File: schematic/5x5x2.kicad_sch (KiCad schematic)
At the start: 158 parts, among them J1 SW Debug, J2 USB_C_Receptacle_USB2.0, SW1 SW, SW11 SW, SW12 SW, SW13 SW, SW14 SW, SW15 SW, SW21 SW, SW22 SW, SW23 SW, SW24 SW, SW25 SW, SW31 SW, SW32 SW, SW33 SW, SW34 SW, SW35 SW, SW41 SW, SW42 SW, SW43 SW, SW44 SW, SW45 SW, SW51 SW, SW52 SW, SW53 SW, SW54 SW, SW55 SW, SW6 ALPS_EC11, U1 SRV0504, U2 STM32F103C8, U3 LD1117S33CTR, Y1 16M

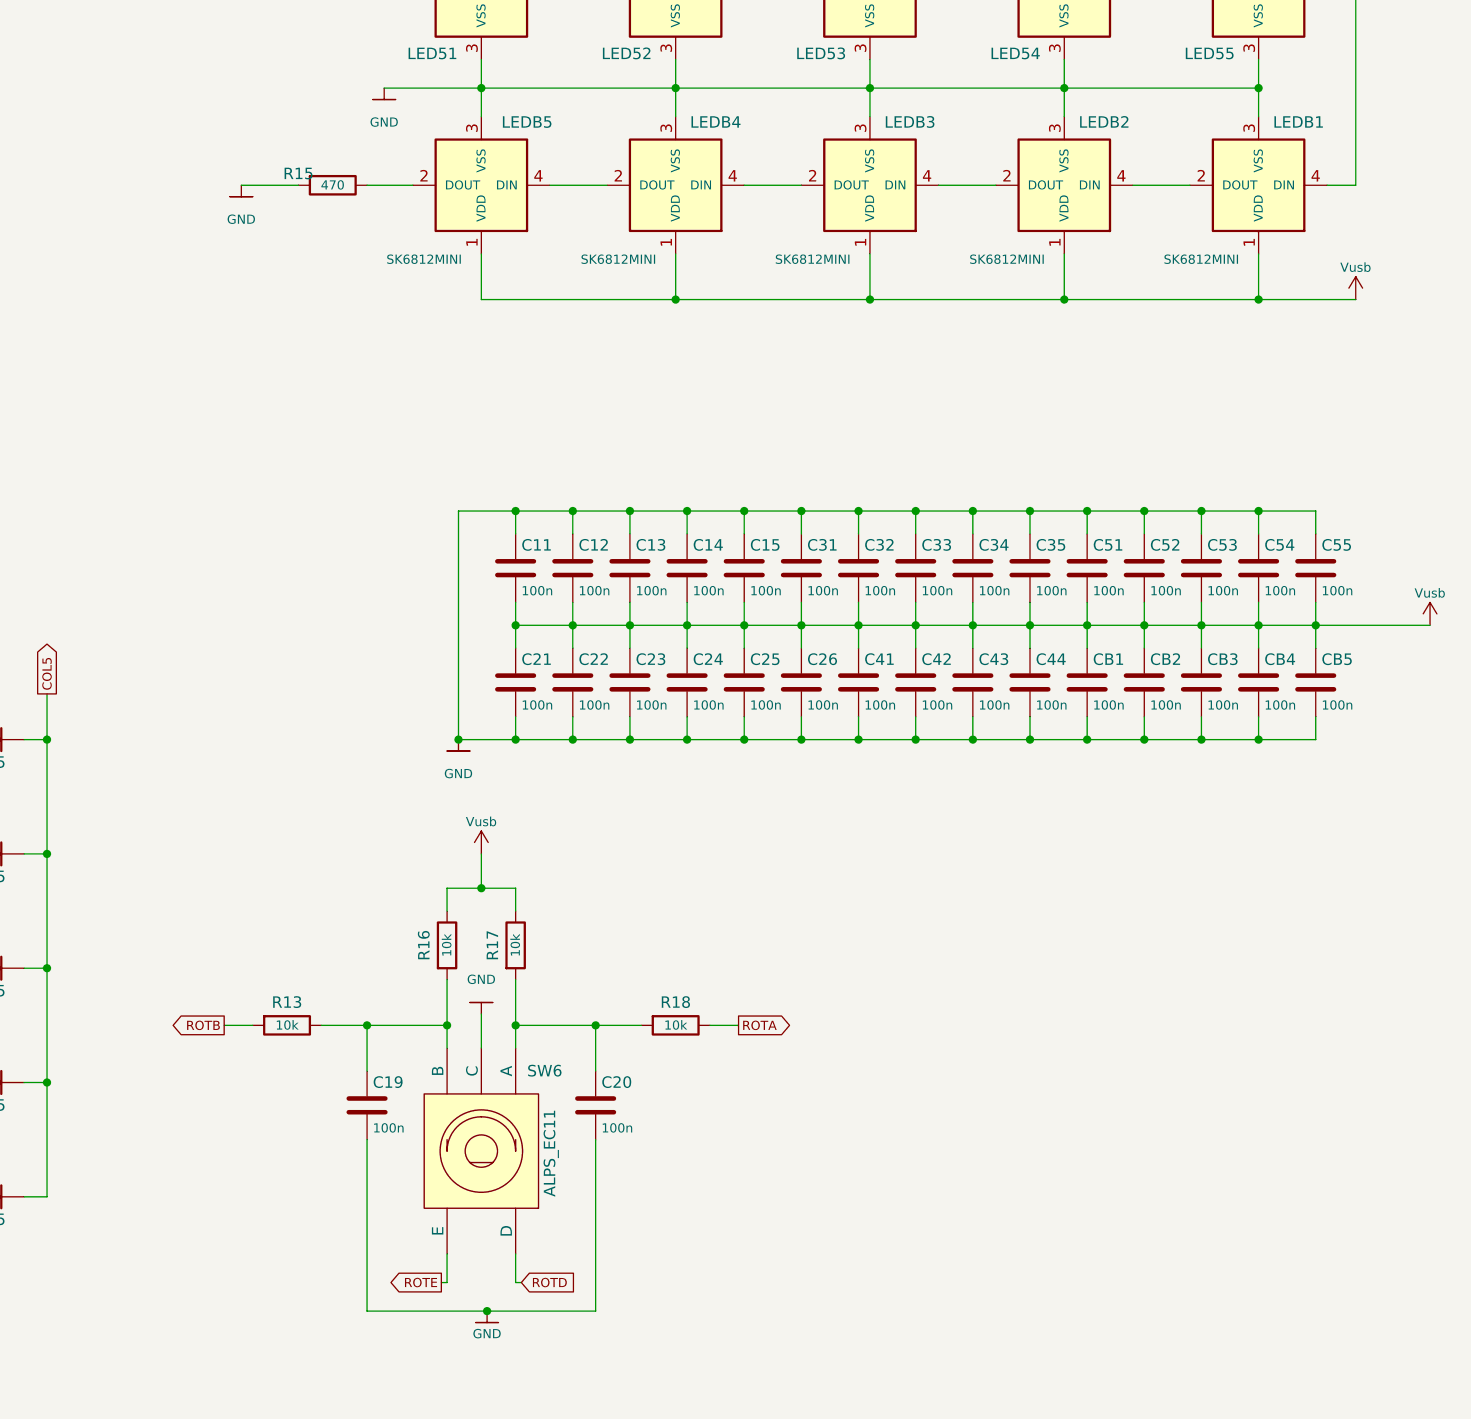
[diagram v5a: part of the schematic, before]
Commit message: Adjusted sk6812 footprint, started routing
Adjusted sk6812 footprint from square cutout to something that is
routable with a mill.

The kailh sockets and leds eat up all the space between the keys. This
means that there is not room for the micro, regulator and usb
receptacle if we stay in a 10x10.

Options:
- Increase size to 11x11 or even 12x12. This would allow for some nice
  mounting holes.

- Make another board beneath the switch board that contains the micro
  and friends.

Lets think about this some more.
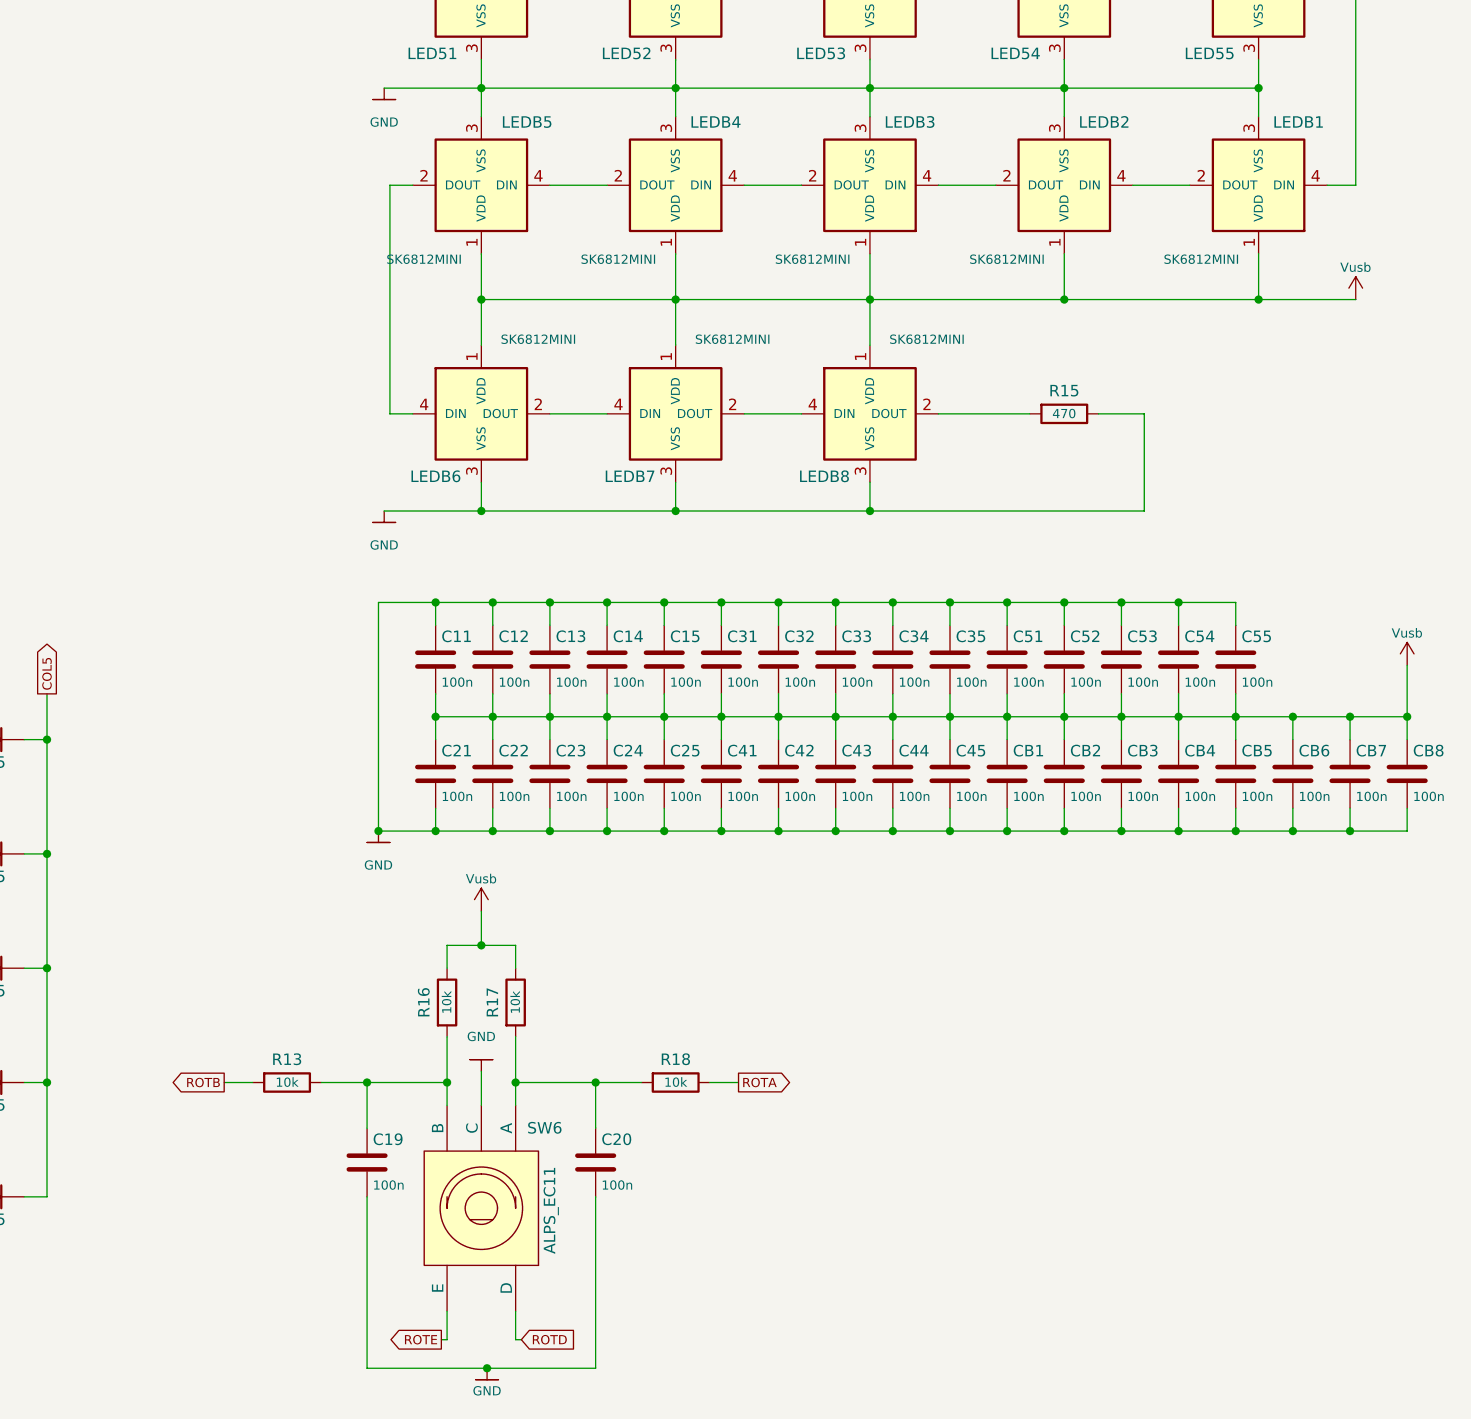
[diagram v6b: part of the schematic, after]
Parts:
- added CB6, CB7, CB8: 100n, Capacitor_SMD:C_0805_2012Metric, symbol Device:C
- added LEDB6, LEDB7, LEDB8: SK6812MINI, footprints:SK6812MINI_rev, symbol SK68xx:SK6812MINI
- C1, C11, C12, C13, C14, C15, C16, C17, C18, C19, C20, C21, C22, C23, C24, C25, C3, C31, C32, C33, C34, C35, C4, C41, C42, C43, C44, C5, C51, C52, C53, C54, C55, C7, C9, CB1, CB2, CB3, CB4, CB5, L1: footprint (none) -> Capacitor_SMD:C_0805_2012Metric
- C10, C2, C6, C8: footprint (none) -> Capacitor_SMD:C_1206_3216Metric
- C45: renamed from C26; footprint (none) -> Capacitor_SMD:C_0805_2012Metric
- C_R1, C_R2, C_R3, R1, R10, R11, R12, R13, R14, R15, R16, R17, R18, R2, R3, R4, R5, R6, R7, R8, R9: footprint (none) -> Resistor_SMD:R_0805_2012Metric
- D1, D2, D3: footprint (none) -> LED_SMD:LED_0805_2012Metric
- J2: footprint (none) -> footprints:USB-C-SMD_TYPE-C-USB-4
- LED11, LED12, LED13, LED14, LED15, LED21, LED22, LED23, LED24, LED25, LED31, LED32, LED33, LED34, LED35, LED41, LED42, LED43, LED44, LED45, LED51, LED52, LED53, LED54, LED55: footprint (none) -> footprints:YS-SK6812MINI-E
- LEDB1, LEDB2, LEDB3, LEDB4, LEDB5: footprint (none) -> footprints:SK6812MINI_rev
- SW1: footprint (none) -> Connector_PinSocket_1.27mm:PinSocket_1x02_P1.27mm_Vertical
- SW11, SW12, SW13, SW14, SW15, SW21, SW22, SW23, SW24, SW25, SW31, SW32, SW33, SW34, SW35, SW41, SW42, SW43, SW44, SW45, SW51, SW52, SW53, SW54, SW55: footprint (none) -> keyswitch:SW_Hotswap_Kailh_MX_1.00u
- SW6: footprint (none) -> footprints:SW-TH_EC11XXXXXXXX
- U1: footprint (none) -> footprints:SOT-23-6_L2.9-W1.6-P0.95-LS2.8-BL
- U2: footprint (none) -> footprints:LQFP-48_L7.0-W7.0-P0.50-LS9.0-BL
- U3: footprint (none) -> footprints:SOT-223-4_L6.5-W3.5-P2.30-LS7.0-BR
- Y1: footprint (none) -> Crystal:Crystal_HC49-U_Vertical
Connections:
- net GND: now also R15.1, CB6.2, CB7.2, CB8.2, LEDB6.3 (VSS), LEDB7.3 (VSS), LEDB8.3 (VSS); no longer R15.2
- net Vusb: now also CB6.1, CB7.1, CB8.1, LEDB6.1 (VDD), LEDB7.1 (VDD), LEDB8.1 (VDD)
- net at LEDB5.2 (DOUT): now also LEDB6.4 (DIN); no longer R15.1
- new net: LEDB8.2 (DOUT), R15.2
- new net: LEDB7.2 (DOUT), LEDB8.4 (DIN)
- new net: LEDB6.2 (DOUT), LEDB7.4 (DIN)
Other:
- moved on the sheet: C11, C12, C13, C14, C15, C19, C20, C21, C22, C23, C24, C25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

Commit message: More routing
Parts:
- renumbered LED25 to LED21, LED24 to LED22, LED22 to LED24, LED21 to LED25, LED45 to LED41, LED44 to LED42, LED42 to LED44, LED41 to LED45
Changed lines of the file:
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@@
   (symbol (lib_id "SK68xx:SK6812MINI-E") (at 355.6 61.595 180) (unit 1)
     (in_bom yes) (on_board yes)
-    (property "Reference" "LED21" (id 0) (at 362.585 54.61 0)
+    (property "Reference" "LED25" (id 0) (at 362.585 54.61 0)
       (effects (font (size 1.27 1.27)) (justify left))
     )
@@
   (symbol (lib_id "SK68xx:SK6812MINI-E") (at 269.24 104.775 180) (unit 1)
     (in_bom yes) (on_board yes)
-    (property "Reference" "LED45" (id 0) (at 276.225 97.79 0)
+    (property "Reference" "LED41" (id 0) (at 276.225 97.79 0)
       (effects (font (size 1.27 1.27)) (justify left))
     )
@@
   (symbol (lib_id "SK68xx:SK6812MINI-E") (at 290.83 61.595 180) (unit 1)
     (in_bom yes) (on_board yes)
-    (property "Reference" "LED24" (id 0) (at 298.45 54.61 0)
+    (property "Reference" "LED22" (id 0) (at 298.45 54.61 0)
       (effects (font (size 1.27 1.27)) (justify left))
     )
@@
   (symbol (lib_id "SK68xx:SK6812MINI-E") (at 290.83 104.775 180) (unit 1)
     (in_bom yes) (on_board yes)
-    (property "Reference" "LED44" (id 0) (at 297.815 97.79 0)
+    (property "Reference" "LED42" (id 0) (at 297.815 97.79 0)
       (effects (font (size 1.27 1.27)) (justify left))
     )
@@
   (symbol (lib_id "SK68xx:SK6812MINI-E") (at 355.6 104.775 180) (unit 1)
     (in_bom yes) (on_board yes)
-    (property "Reference" "LED41" (id 0) (at 362.585 97.79 0)
+    (property "Reference" "LED45" (id 0) (at 362.585 97.79 0)
       (effects (font (size 1.27 1.27)) (justify left))
     )
@@
   (symbol (lib_id "SK68xx:SK6812MINI-E") (at 334.01 61.595 180) (unit 1)
     (in_bom yes) (on_board yes)
-    (property "Reference" "LED22" (id 0) (at 340.995 54.61 0)
+    (property "Reference" "LED24" (id 0) (at 340.995 54.61 0)
       (effects (font (size 1.27 1.27)) (justify left))
     )
@@
   (symbol (lib_id "SK68xx:SK6812MINI-E") (at 334.01 104.775 180) (unit 1)
     (in_bom yes) (on_board yes)
-    (property "Reference" "LED42" (id 0) (at 340.995 97.79 0)
+    (property "Reference" "LED44" (id 0) (at 340.995 97.79 0)
       (effects (font (size 1.27 1.27)) (justify left))
     )
@@
   (symbol (lib_id "SK68xx:SK6812MINI-E") (at 269.24 61.595 180) (unit 1)
     (in_bom yes) (on_board yes)
-    (property "Reference" "LED25" (id 0) (at 276.86 54.61 0)
+    (property "Reference" "LED21" (id 0) (at 276.86 54.61 0)
       (effects (font (size 1.27 1.27)) (justify left))
     )
@@
       (reference "LED15") (unit 1) (value "SK6812MINI-E") (footprint "footprints:YS-SK6812MINI-E")
     )
-    (path "/025174a1-c1b3-43da-9711-d3a3a7ce445e"
+    (path "/f51d1fbb-e25c-4749-bba5-7561a1e13b31"
       (reference "LED21") (unit 1) (value "SK6812MINI-E") (footprint "footprints:YS-SK6812MINI-E")
     )
-    (path "/dd1c2f7a-c2b3-4df2-93b2-04fe1591f702"
+    (path "/3abfbcd0-9099-438c-a966-1761d5740cb1"
       (reference "LED22") (unit 1) (value "SK6812MINI-E") (footprint "footprints:YS-SK6812MINI-E")
     )
@@
       (reference "LED23") (unit 1) (value "SK6812MINI-E") (footprint "footprints:YS-SK6812MINI-E")
     )
-    (path "/3abfbcd0-9099-438c-a966-1761d5740cb1"
+    (path "/dd1c2f7a-c2b3-4df2-93b2-04fe1591f702"
       (reference "LED24") (unit 1) (value "SK6812MINI-E") (footprint "footprints:YS-SK6812MINI-E")
     )
-    (path "/f51d1fbb-e25c-4749-bba5-7561a1e13b31"
+    (path "/025174a1-c1b3-43da-9711-d3a3a7ce445e"
       (reference "LED25") (unit 1) (value "SK6812MINI-E") (footprint "footprints:YS-SK6812MINI-E")
     )
@@
       (reference "LED35") (unit 1) (value "SK6812MINI-E") (footprint "footprints:YS-SK6812MINI-E")
     )
-    (path "/d96937f5-5821-40dc-9935-d17c504b3d87"
+    (path "/0e23ae1d-611b-4654-9b36-886c92306d44"
       (reference "LED41") (unit 1) (value "SK6812MINI-E") (footprint "footprints:YS-SK6812MINI-E")
     )
-    (path "/f1adb53e-37ad-4a2f-81ba-8714ff14ec13"
+    (path "/72abcb82-0f94-41d1-ace4-f1ac54bc9c8d"
       (reference "LED42") (unit 1) (value "SK6812MINI-E") (footprint "footprints:YS-SK6812MINI-E")
     )
@@
       (reference "LED43") (unit 1) (value "SK6812MINI-E") (footprint "footprints:YS-SK6812MINI-E")
     )
-    (path "/72abcb82-0f94-41d1-ace4-f1ac54bc9c8d"
+    (path "/f1adb53e-37ad-4a2f-81ba-8714ff14ec13"
       (reference "LED44") (unit 1) (value "SK6812MINI-E") (footprint "footprints:YS-SK6812MINI-E")
     )
-    (path "/0e23ae1d-611b-4654-9b36-886c92306d44"
+    (path "/d96937f5-5821-40dc-9935-d17c504b3d87"
       (reference "LED45") (unit 1) (value "SK6812MINI-E") (footprint "footprints:YS-SK6812MINI-E")
     )

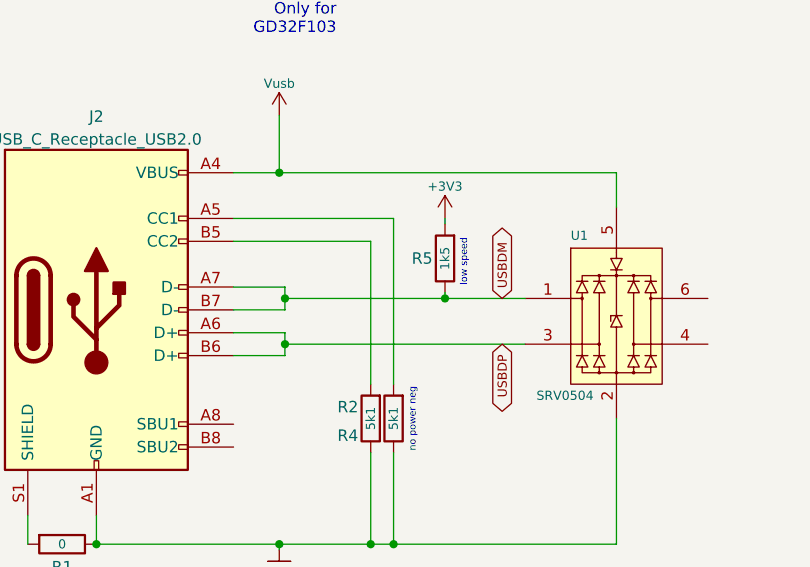
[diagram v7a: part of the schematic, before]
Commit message: Routed for mcu on other pcb
This way we can stay with 2 layers, and optionally have an additional
pcb for just the key switches without kailh holders.
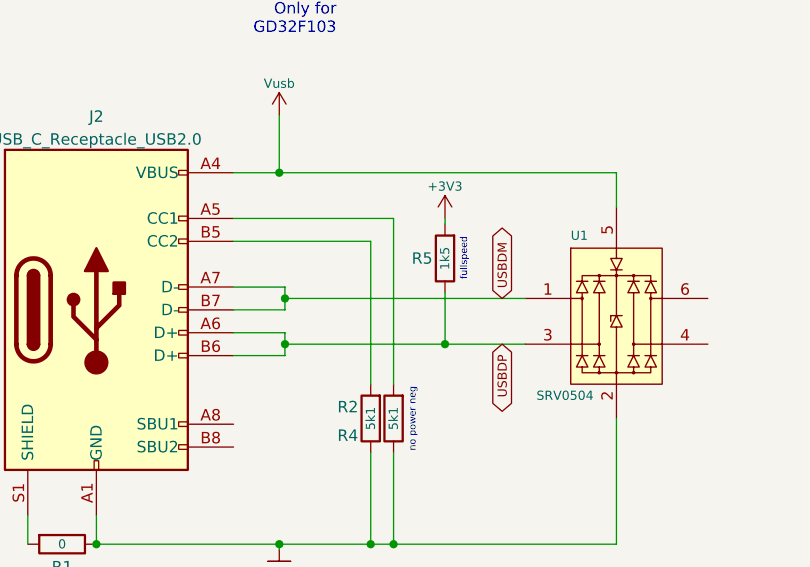
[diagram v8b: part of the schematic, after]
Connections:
- net USBDM: no longer R5.1
- net USBDP: now also R5.1
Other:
- note added: "fullspeed"
- note removed: "low speed"
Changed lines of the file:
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@@
   (junction (at 269.24 160.655) (diameter 0) (color 0 0 0 0)
   )
-  (junction (at 74.295 164.465) (diameter 0) (color 0 0 0 0)
-  )
   (junction (at 182.88 234.95) (diameter 0) (color 0 0 0 0)
   )
@@
   (junction (at 270.51 219.71) (diameter 0) (color 0 0 0 0)
   )
+  (junction (at 74.295 169.545) (diameter 0) (color 0 0 0 0)
+  )
   (junction (at 116.84 265.43) (diameter 0) (color 0 0 0 0)
   )
@@
     (stroke (width 0) (type default) (color 0 0 0 0))
   )
-  (wire (pts (xy 74.295 163.83) (xy 74.295 164.465))
-    (stroke (width 0) (type default) (color 0 0 0 0))
-  )
   (wire (pts (xy 56.515 170.815) (xy 50.8 170.815))
     (stroke (width 0) (type default) (color 0 0 0 0))
@@
     (stroke (width 0) (type default) (color 0 0 0 0))
   )
-  (wire (pts (xy 56.515 164.465) (xy 74.295 164.465))
+  (wire (pts (xy 56.515 164.465) (xy 83.185 164.465))
     (stroke (width 0) (type default) (color 0 0 0 0))
   )
@@
     (stroke (width 0) (type default) (color 0 0 0 0))
   )
-  (wire (pts (xy 74.295 164.465) (xy 83.185 164.465))
-    (stroke (width 0) (type default) (color 0 0 0 0))
-  )
   (wire (pts (xy 55.88 81.28) (xy 55.88 83.82))
     (stroke (width 0) (type default) (color 0 0 0 0))
@@
     (stroke (width 0) (type default) (color 0 0 0 0))
   )
+  (wire (pts (xy 74.295 163.83) (xy 74.295 169.545))
+    (stroke (width 0) (type default) (color 0 0 0 0))
+  )
   (wire (pts (xy 144.78 222.25) (xy 144.78 234.95))
     (stroke (width 0) (type default) (color 0 0 0 0))
@@
     (stroke (width 0) (type default) (color 0 0 0 0))
   )
-  (wire (pts (xy 56.515 169.545) (xy 83.185 169.545))
+  (wire (pts (xy 56.515 169.545) (xy 74.295 169.545))
     (stroke (width 0) (type default) (color 0 0 0 0))
   )
@@
     (stroke (width 0) (type default) (color 0 0 0 0))
   )
+  (wire (pts (xy 74.295 169.545) (xy 83.185 169.545))
+    (stroke (width 0) (type default) (color 0 0 0 0))
+  )
   (wire (pts (xy 334.01 133.985) (xy 334.01 137.16))
     (stroke (width 0) (type default) (color 0 0 0 0))
@@
   (wire (pts (xy 340.36 219.71) (xy 340.36 217.17))
     (stroke (width 0) (type default) (color 0 0 0 0))
+  )
+  (text "fullspeed" (at 76.835 162.56 90)
+    (effects (font (size 0.762 0.762)) (justify left bottom))
   )
   (text "Only for \nMM32F103" (at 196.215 127 0)
@@
     (effects (font (size 1.27 1.27)) (justify right bottom))
   )
-  (text "low speed" (at 76.835 163.195 90)
-    (effects (font (size 0.762 0.762)) (justify left bottom))
-  )
   (text "no power neg" (at 71.12 181.61 90)
